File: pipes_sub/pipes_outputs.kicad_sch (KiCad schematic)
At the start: 72 parts, among them U20 GLV5549, U21 GLV5549, U22 GLV5549, U23 TL072CP, U24 TL072CP, U25 TL072CP, U26 GLV5549, U27 GLV5549, U28 GLV5549, U29 TL072CP, U30 TL072CP, U31 TL072CP, U32 GLV5549, U33 GLV5549, U34 TL072CP, U35 TL072CP

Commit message: Changes labels: VCO to SIG
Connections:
- net VCO1 renamed SIG1
- net VCO2 renamed SIG2
- net VCO3 renamed SIG3
- net VCO4 renamed SIG4
- net VCO5 renamed SIG5
- net VCO6 renamed SIG6
- net VCO7 renamed SIG7
- net VCO8 renamed SIG8
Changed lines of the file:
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@@
     )
   )
-  (global_label "VCO2" (shape output) (at 163.83 137.16 0) (fields_autoplaced)
+  (global_label "SIG2" (shape output) (at 163.83 137.16 0) (fields_autoplaced)
     (effects (font (size 1.27 1.27)) (justify left))
     (property "Intersheet References" "${INTERSHEET_REFS}" (id 0) (at 171.1417 137.0806 0)
@@
     )
   )
-  (global_label "VCO7" (shape output) (at 164.2012 35.4881 0) (fields_autoplaced)
+  (global_label "SIG7" (shape output) (at 164.2012 35.4881 0) (fields_autoplaced)
     (effects (font (size 1.27 1.27)) (justify left))
     (property "Intersheet References" "${INTERSHEET_REFS}" (id 0) (at 171.5129 35.4087 0)
@@
     )
   )
-  (global_label "VCO8" (shape output) (at 247.269 35.56 0) (fields_autoplaced)
+  (global_label "SIG8" (shape output) (at 247.269 35.56 0) (fields_autoplaced)
     (effects (font (size 1.27 1.27)) (justify left))
     (property "Intersheet References" "${INTERSHEET_REFS}" (id 0) (at 254.5807 35.4806 0)
@@
     )
   )
-  (global_label "VCO3" (shape output) (at 83.185 88.9 0) (fields_autoplaced)
+  (global_label "SIG3" (shape output) (at 83.185 88.9 0) (fields_autoplaced)
     (effects (font (size 1.27 1.27)) (justify left))
     (property "Intersheet References" "${INTERSHEET_REFS}" (id 0) (at 90.4967 88.8206 0)
@@
     )
   )
-  (global_label "VCO6" (shape output) (at 83.185 35.56 0) (fields_autoplaced)
+  (global_label "SIG6" (shape output) (at 83.185 35.56 0) (fields_autoplaced)
     (effects (font (size 1.27 1.27)) (justify left))
     (property "Intersheet References" "${INTERSHEET_REFS}" (id 0) (at 90.4967 35.4806 0)
@@
     )
   )
-  (global_label "VCO1" (shape output) (at 83.185 137.16 0) (fields_autoplaced)
+  (global_label "SIG1" (shape output) (at 83.185 137.16 0) (fields_autoplaced)
     (effects (font (size 1.27 1.27)) (justify left))
     (property "Intersheet References" "${INTERSHEET_REFS}" (id 0) (at 90.4967 137.0806 0)
@@
     )
   )
-  (global_label "VCO5" (shape output) (at 247.904 88.9 0) (fields_autoplaced)
+  (global_label "SIG5" (shape output) (at 247.904 88.9 0) (fields_autoplaced)
     (effects (font (size 1.27 1.27)) (justify left))
     (property "Intersheet References" "${INTERSHEET_REFS}" (id 0) (at 255.2157 88.8206 0)
@@
     )
   )
-  (global_label "VCO4" (shape output) (at 165.735 88.9 0) (fields_autoplaced)
+  (global_label "SIG4" (shape output) (at 165.735 88.9 0) (fields_autoplaced)
     (effects (font (size 1.27 1.27)) (justify left))
     (property "Intersheet References" "${INTERSHEET_REFS}" (id 0) (at 173.0467 88.8206 0)

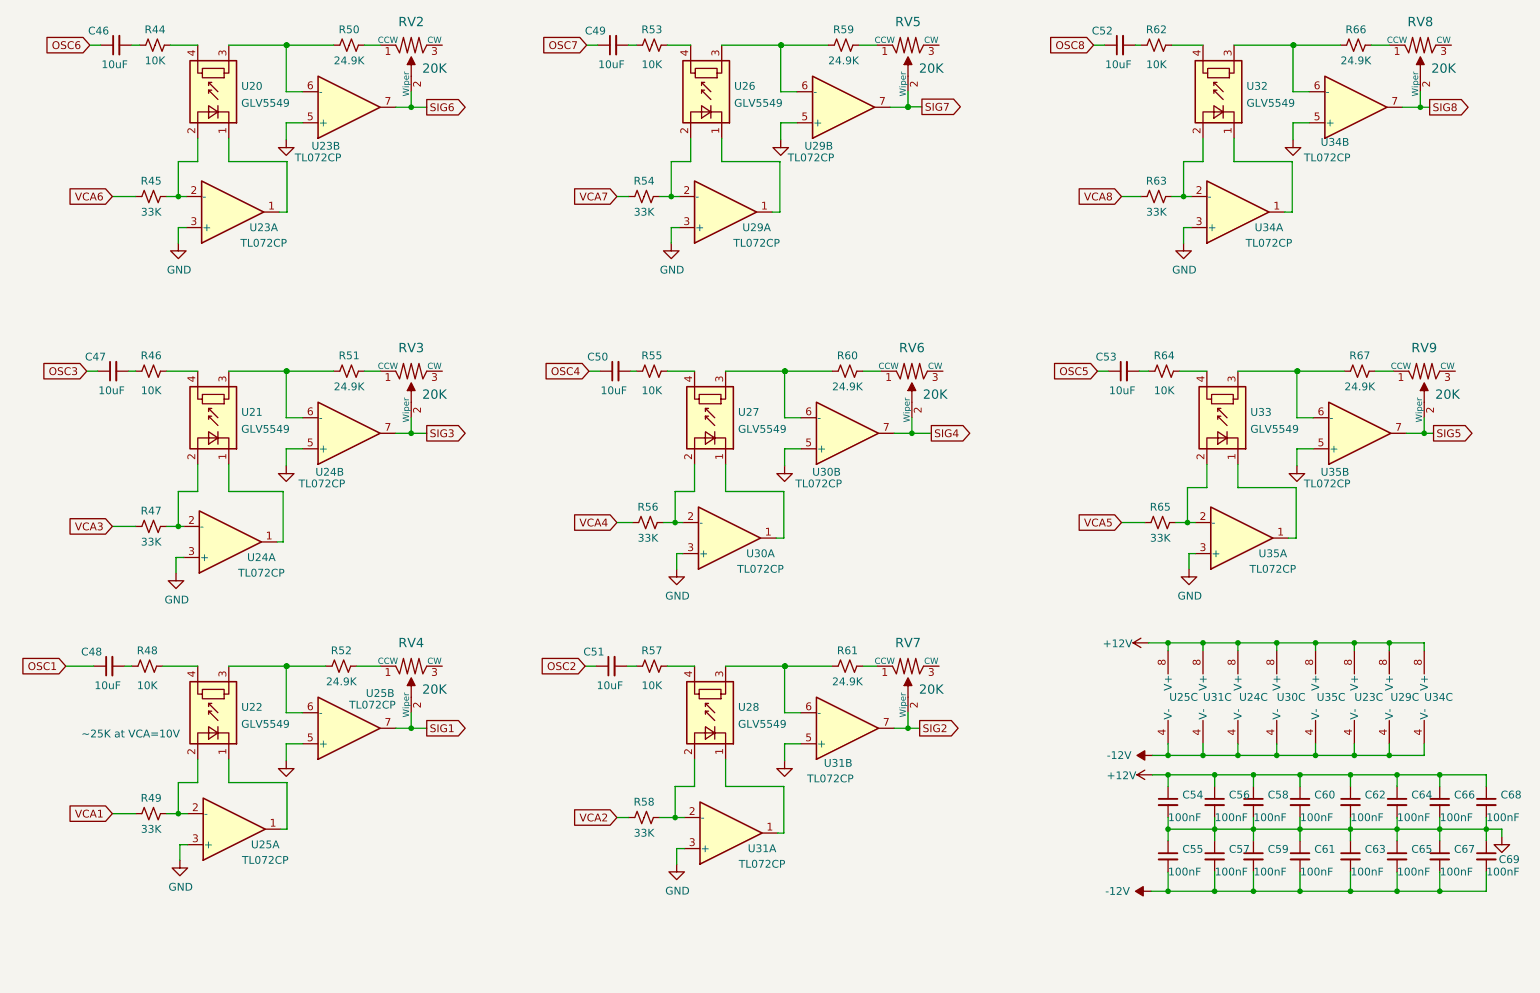
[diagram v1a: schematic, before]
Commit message: Version 1.1 of boards
Changes to use NSL-32SR3 Vactrols
Fixes 3904 package
Adds 10-step waveform
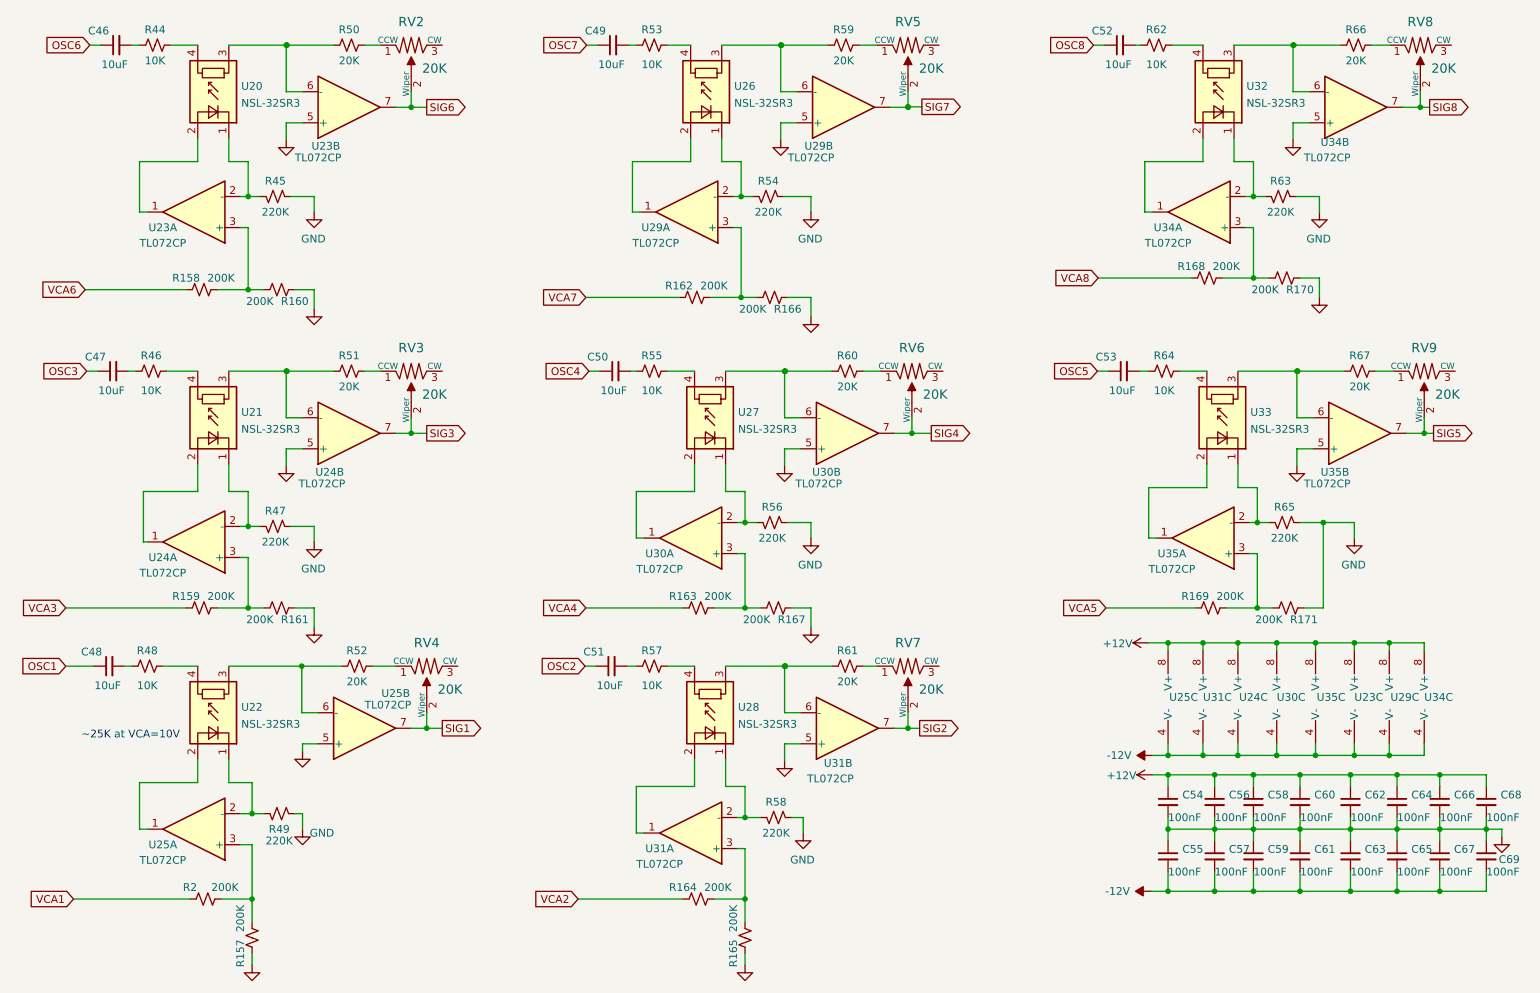
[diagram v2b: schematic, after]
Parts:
- added R157, R158, R159, R160, R161, R162, R163, R164, R165, R166, R167, R168, R169, R170, R171, R2: 200K, Resistor_SMD:R_0603_1608Metric, symbol Device:R_Small_US
- R45, R47, R49, R54, R56, R58, R63, R65: value 33K -> 220K; LCSC Part # C4216 -> C22961
- R50, R51, R52, R59, R60, R61, R66, R67: value 24.9K -> 20K; LCSC Part # C137761 -> C4184
- RV2, RV3, RV4, RV5, RV6, RV7, RV8, RV9: footprint sputterizer:Potentiometer_Bourns_3224W_Vertical -> Potentiometer_SMD:Potentiometer_Bourns_3224W_Vertical
- U20, U21, U22, U26, U27, U28, U32, U33: value GLV5549 -> NSL-32SR3; Digi-Key Part (none) -> NSL-32SR3-ND
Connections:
- net GND: now also R45.2, R47.2, R49.2, R54.2, R56.2, R58.2, R63.2, R65.2, R157.1, R160.1, R161.1, R165.1, R166.1, R167.1, R170.1, R171.1; no longer U23.3 (+), U24.3 (+), U25.3 (+), U29.3 (+), U30.3 (+), U31.3 (+), U34.3 (+), U35.3 (+)
- net VCA1: now also R2.1; no longer R49.2
- net VCA2: now also R164.1; no longer R58.2
- net VCA3: now also R159.1; no longer R47.2
- net VCA4: now also R163.1; no longer R56.2
- net VCA5: now also R169.1; no longer R65.2
- net VCA6: now also R158.1; no longer R45.2
- net VCA7: now also R162.1; no longer R54.2
- net VCA8: now also R168.1; no longer R63.2
- net at U30.1: now also U27.2 (+); no longer U27.1 (-)
- net at R56.1, U30.2 (-): now also U27.1 (-); no longer U27.2 (+)
- net at U32.1 (-): now also R63.1, U34.2 (-); no longer U34.1
- net at U22.1 (-): now also R49.1, U25.2 (-); no longer U25.1
- net at R47.1, U24.2 (-): now also U21.1 (-); no longer U21.2 (+)
- net at U33.1 (-): now also R65.1, U35.2 (-); no longer U35.1
- net at U31.1: now also U28.2 (+); no longer U28.1 (-)
- net at R58.1, U31.2 (-): now also U28.1 (-); no longer U28.2 (+)
- net at U29.1: now also U26.2 (+); no longer U26.1 (-)
- net at R54.1, U29.2 (-): now also U26.1 (-); no longer U26.2 (+)
- net at R45.1, U23.2 (-): now also U20.1 (-); no longer U20.2 (+)
- net at U24.1: now also U21.2 (+); no longer U21.1 (-)
- net at U23.1: now also U20.2 (+); no longer U20.1 (-)
- new net: R163.2, R167.2, U30.3 (+)
- new net: R164.2, R165.2, U31.3 (+)
- new net: R159.2, R161.2, U24.3 (+)
- new net: R157.2, R2.2, U25.3 (+)
- new net: U32.2 (+), U34.1
- new net: R168.2, R170.2, U34.3 (+)
- new net: R158.2, R160.2, U23.3 (+)
- new net: U22.2 (+), U25.1
- new net: U33.2 (+), U35.1
- new net: R162.2, R166.2, U29.3 (+)
- new net: R169.2, R171.2, U35.3 (+)
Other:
- moved on the sheet: R45, R47, R49, R52, R54, R56, R58, R63, R65, RV4, U23A, U24A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

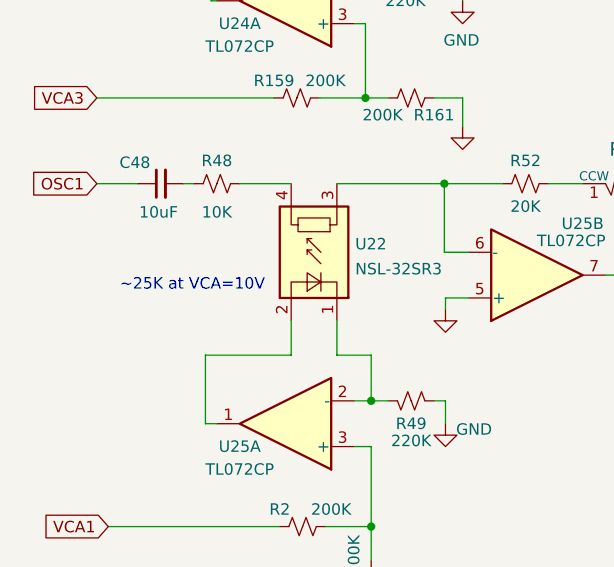
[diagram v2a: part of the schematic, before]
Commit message: Changed note on vactrol resistance.
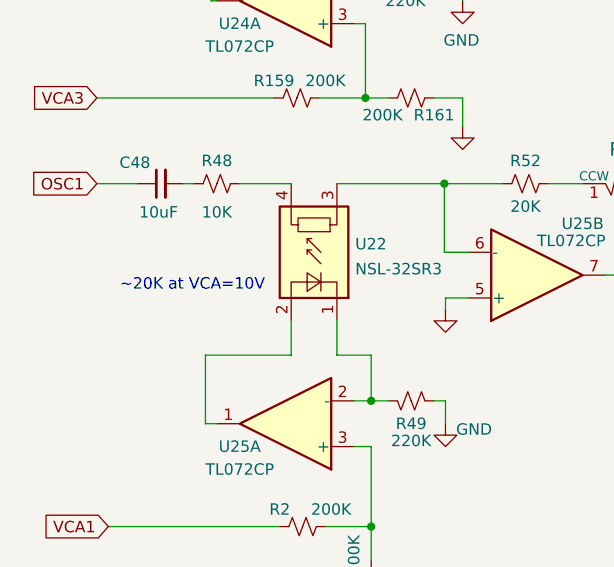
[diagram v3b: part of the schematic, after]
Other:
- note added: "~20K at VCA=10V"
- note removed: "~25K at VCA=10V"
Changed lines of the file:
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@@
     (stroke (width 0) (type default) (color 0 0 0 0))
   )
-  (text "~25K at VCA=10V" (at 26.67 139.065 0)
+  (text "~20K at VCA=10V" (at 26.67 139.065 0)
     (effects (font (size 1.27 1.27)) (justify left bottom))
   )

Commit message: Uses new vactrols.
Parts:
- removed R44, R46, R48, R53, R55, R57, R62, R64: 10K, Resistor_SMD:R_0603_1608Metric, symbol Device:R_Small_US
- C46, C47, C48, C49, C50, C51, C52, C53: value 10uF -> 22uF; LCSC Part # C15850 -> C277470
- R45, R47, R49, R54, R56, R58, R63, R65: value 220K -> 20K; LCSC Part # C22961 -> C136589
- R50, R51, R52, R59, R60, R61, R66, R67: value 20K -> 430; LCSC Part # C4184 -> C23170
- RV2: value 20K -> 500; Digi-Key Part 3224W-203ECT-ND -> (none); LCSC Part # C55071 -> C116324
- RV3, RV4, RV5, RV6, RV7, RV8, RV9: value 20K -> 500; Digi-Key Part 490-2881-ND -> (none); LCSC Part # C55071 -> C116324
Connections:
- net at C51.2: now also U28.4
- net at C53.2: now also U33.4
- net at C48.2: now also U22.4
- net at U27.4: now also C50.2
- net at C52.2: now also U32.4
- net at C49.2: now also U26.4
- net at C46.2: now also U20.4
- net at C47.2: now also U21.4
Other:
- note added: "Bump 9V sig to 10V Gain = 1.111"
- note added: "~600 ohms at VCA=10V range: 400 - 800"
- note removed: "~20K at VCA=10V"
- company: (none) -> Greenface Labs
